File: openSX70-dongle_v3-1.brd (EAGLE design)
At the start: 47.1 x 24.7 mm, 26 parts

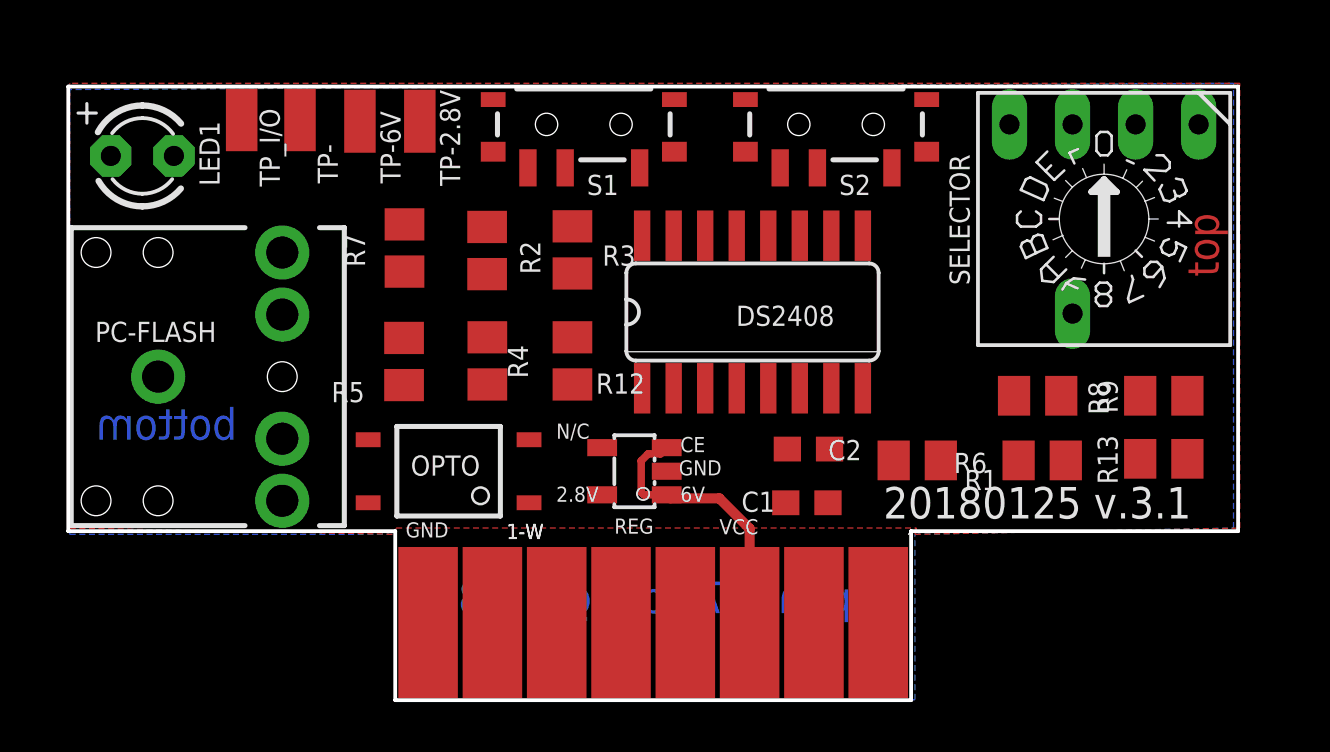
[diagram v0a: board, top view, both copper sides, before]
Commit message: Added a 2.8V regulator needed to work with the 2.5V arduino. Removed R13 and R6 (pullup resistors to VCC for LED and opto), since they were not needed.
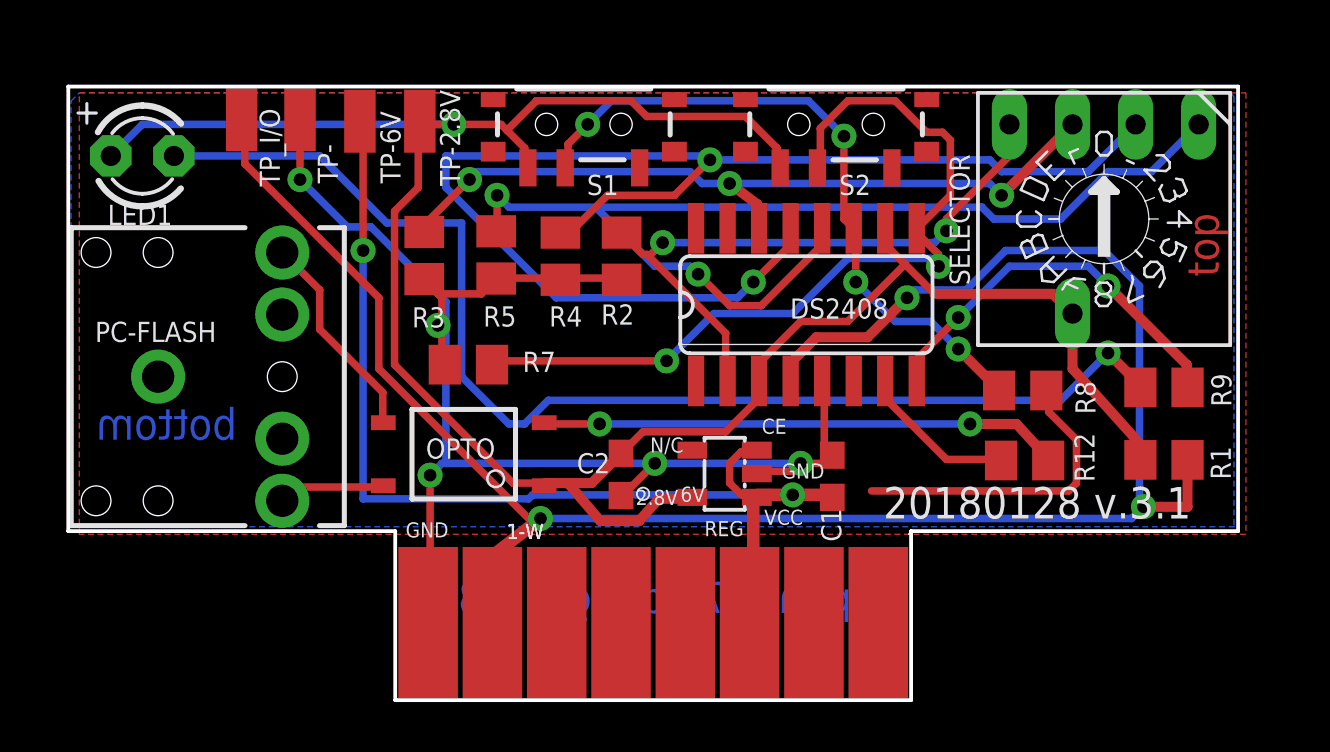
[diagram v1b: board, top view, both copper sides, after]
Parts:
- removed R13, R6: 100K, rcl:M0805
- moved R12 18.6 mm to (40.6, 10.6), turned to 0 degrees
- moved R1 9.94 mm to (46.2, 10.6)
- moved C2 7.62 mm to (24.4, 10.0), turned to 270 degrees
- moved R3 5.97 mm to (16.4, 18.8)
- moved R5 5.67 mm to (19.3, 18.9), turned to 90 degrees
- moved R2 5.42 mm to (24.4, 18.8), turned to 270 degrees
- moved R7 5.36 mm to (18.2, 14.5), turned to 180 degrees
- moved R4 5.14 mm to (21.9, 18.8)
- moved REG 3.63 mm to (28.5, 10.1)
- moved DS2408 2.19 mm to (31.8, 16.9)
- moved C1 1.48 mm to (32.9, 9.96), turned to 90 degrees
- moved OPTO 0.92 mm to (18.0, 10.2)
- moved R8 0.64 mm to (40.5, 13.4)
- moved R9 0.34 mm to (46.2, 13.5)
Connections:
- net 2.8V: no longer R13.2, R6.2
- net N$11: no longer R6.1
- net N$8: no longer R13.1
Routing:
- net 2.8V: track 0.00 -> 92.8 mm, vias 0 -> 1
- net N$1: track 0.00 -> 81.1 mm, vias 0 -> 3
- net GND: track 0.00 -> 72.3 mm, vias 0 -> 5
- net N$5: track 0.00 -> 54.6 mm, vias 0 -> 2
- net N$2: track 0.00 -> 48.8 mm, vias 0 -> 1
- net N$13: track 0.00 -> 44.1 mm, vias 0 -> 2
- net N$7: track 0.00 -> 34.1 mm, vias 0 -> 2
- net VCC: track 11.3 -> 44.5 mm, vias 0 -> 2
- net N$4: track 0.00 -> 31.3 mm, vias 0 -> 3
- net N$6: track 0.00 -> 27.2 mm, vias 0 -> 4
- net N$3: track 0.00 -> 25.6 mm, vias 0 -> 2
- net N$10: track 0.00 -> 21.1 mm, vias 0 -> 2
- net N$8: track 0.00 -> 15.9 mm, vias 0 -> 2
- net N$15: track 0.00 -> 8.53 mm
- net N$11: track 0.00 -> 6.37 mm
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- added copper zone on layer 16, net N$9
- removed copper zone on layer 16, net GND
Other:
- board text added: "20180128 v.3.1"
- board text removed: "20180125 v.3.1"

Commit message: changes
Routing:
- net GND: track 72.3 -> 59.7 mm
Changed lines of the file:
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@@
 <element name="REG" library="openSX70" package="SOT-23-5" value="NCP4688" x="28.5322" y="10.0584" smashed="yes" rot="R90">
 <attribute name="NAME" x="29.3022" y="8.1534" size="0.6096" layer="25" font="vector" rot="R180"/>
-<attribute name="VALUE" x="29.8022" y="12.5984" size="0.889" layer="27" ratio="11" rot="R180"/>
+<attribute name="VALUE" x="29.8022" y="12.5984" size="0.6096" layer="27" font="vector" ratio="11" rot="R180"/>
 </element>
 <element name="TP-6V" library="wirepad" library_urn="urn:adsk.eagle:library:412" package="SMD1,27-2,54" package3d_urn="urn:adsk.eagle:package:30839/1" value="" x="13.843" y="24.257" smashed="yes">
@@
 <attribute name="NAME" x="33.2326" y="7.3218" size="0.8128" layer="25" font="vector" rot="R90"/>
 <attribute name="SPICEPREFIX" value="C" x="32.8676" y="9.9568" size="1.778" layer="27" rot="R90" display="off"/>
-<attribute name="VALUE" x="34.7726" y="9.3218" size="1.27" layer="27" rot="R90"/>
+<attribute name="VALUE" x="34.7726" y="9.3218" size="0.6096" layer="27" rot="R90"/>
 </element>
 <element name="C2" library="rcl" library_urn="urn:adsk.eagle:library:334" package="C0603" package3d_urn="urn:adsk.eagle:package:23616/2" value="1.0uF" x="24.3586" y="10.033" smashed="yes" rot="R270">
 <attribute name="NAME" x="22.5792" y="10.0744" size="0.8128" layer="25" font="vector"/>
 <attribute name="SPICEPREFIX" value="C" x="24.3586" y="10.033" size="1.778" layer="27" rot="R270" display="off"/>
-<attribute name="VALUE" x="22.4536" y="10.668" size="1.27" layer="27" rot="R270"/>
+<attribute name="VALUE" x="22.4536" y="10.668" size="0.6096" layer="27" rot="R270"/>
 </element>
 </elements>
@@
 <wire x1="31.59125" y1="10.4775" x2="31.27375" y2="10.16" width="0.3048" layer="1"/>
 <wire x1="29.845" y1="10.16" x2="29.8323" y2="10.0584" width="0.3048" layer="1"/>
-<wire x1="41.5925" y1="12.54125" x2="41.5925" y2="13.335" width="0.3048" layer="1"/>
-<wire x1="42.70375" y1="11.43" x2="41.5925" y2="12.54125" width="0.3048" layer="1"/>
-<wire x1="42.70375" y1="9.68375" x2="42.70375" y2="11.43" width="0.3048" layer="1"/>
-<wire x1="42.38625" y1="9.36625" x2="42.70375" y2="9.68375" width="0.3048" layer="1"/>
-<wire x1="34.44875" y1="9.36625" x2="42.38625" y2="9.36625" width="0.3048" layer="1"/>
-<wire x1="41.5925" y1="13.335" x2="41.4884" y2="13.4112" width="0.3048" layer="1"/>
 <wire x1="33.02" y1="10.795" x2="32.8676" y2="10.8068" width="0.3048" layer="1"/>
 <wire x1="32.54375" y1="10.63625" x2="32.54375" y2="13.6525" width="0.3048" layer="1"/>
